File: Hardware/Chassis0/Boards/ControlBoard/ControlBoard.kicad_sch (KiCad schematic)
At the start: 18 parts, among them J1 TBP02R2W-381-06BE, J11 Conn_02x10_Counter_Clockwise, J12 Conn_02x10_Counter_Clockwise, J13 Conn_02x10_Counter_Clockwise, J14 Conn_02x10_Counter_Clockwise, J2 TBP02R2W-381-06BE, J3 TBP01R2W-508-02BE, J4 TBP01R1-508-04BE, J5 Conn_02x10_Counter_Clockwise, J7 TBP02R2W-381-08BE, J8 TBP02R2W-381-08BE

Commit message: Update size 0 cad model
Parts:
- removed J11, J12, J13, J14, J5: Conn_02x10_Counter_Clockwise, Connector_PinSocket_2.54mm:PinSocket_2x10_P2.54mm_Vertical, symbol Connector_Generic:Conn_02x10_Counter_Clockwise
- removed J4: TBP01R1-508-04BE, InverterCom:TBP01R150804BE, symbol InverterCom:TBP01R1-508-04BE
- removed J8: TBP02R2W-381-08BE, InverterCom:TBP02R2W38108BE, symbol InverterCom:TBP02R2W-381-08BE
- added J5, J6, J8, J9: Conn_02x08_Counter_Clockwise, Connector_PinSocket_2.54mm:PinSocket_2x08_P2.54mm_Vertical, symbol Connector_Generic:Conn_02x08_Counter_Clockwise
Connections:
- net HEATSINK_TMP_V: now also J9.16 (Pin_16)
- net CAN/CAN_L_B: now reaches J7.3
- net CAN/CAN_JMP_B: now reaches J7.5
- net +5V_V renamed +5V_C
- net +5V_C: now also J9.14 (Pin_14)
- net CAN_24V_OUT renamed CAN/CAN_JMP_A
- net CAN_GND: no longer names the net of J7.8
- net CAN_HIGH: no longer names the net of J7.7
- net CAN_JUMPER_A renamed CAN/CAN_H_B
- net CAN_JUMPER_B renamed CAN/CAN_GND
- net CAN_LOW: no longer names the net of J7.6
- net GND_V renamed GND_C
- net GND_C: now also J9.1 (Pin_1)
- new net +5V_Y: J9.4 (Pin_4)
- new net DC_LINK_VSENSE_U: J5.16 (Pin_16)
- new net GND_U: J5.4 (Pin_4)
- new net GND_Y: J9.2 (Pin_2)
- new net ISENSE_DC_LINK_Y: J9.6 (Pin_6)
- new net ISENSE_PH_U_Y: J9.8 (Pin_8)
- new net ISENSE_PH_V_Y: J9.10 (Pin_10)
- new net ISENSE_PH_W_Y: J9.12 (Pin_12)
- new net PH_U_H_G: J5.12 (Pin_12)
- new net PH_U_H_S: J5.14 (Pin_14)
- new net PH_U_L_D: J5.6 (Pin_6)
- new net PH_U_L_G: J5.2 (Pin_2)
- new net PH_V_H_D: J6.16 (Pin_16)
- new net PH_V_H_G: J6.12 (Pin_12)
- new net PH_V_H_S: J6.14 (Pin_14)
- new net PH_V_L_D: J6.6 (Pin_6)
- new net PH_V_L_G: J6.2 (Pin_2)
- new net PH_V_L_S: J6.4 (Pin_4)
- new net PH_W_H_D: J8.16 (Pin_16)
- new net PH_W_H_G: J8.12 (Pin_12)
- new net PH_W_H_S: J8.14 (Pin_14)
- new net PH_W_L_D: J8.6 (Pin_6)
- new net PH_W_L_G: J8.2 (Pin_2)
- new net PH_W_L_S: J8.4 (Pin_4)
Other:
- added sheet ADC_1 (ADC1.kicad_sch)
- added sheet CAN (CAN.kicad_sch)
- added sheet GateDriverAssembly (GateDriverAssembly.kicad_sch)
- sheet Control ports: added none; removed RELAY1_A, RELAY2_A, RELAY3_A
- note removed: "CANBUS OUTPUT CONNECTOR TO CONTROL BOARD INTERFACES TO OUTSIDE WORLD"
- note removed: "CONNECTION FROM MAINBOARD TO CONTROL MODULE ABOVE PROVIDES RELAY OUTPUTS + GATE DRIVER INTERLOCK"
- note removed: "CONNECTOR FROM MAIN BOARD TO CONTROL MODULE ABOVE ADC SPI INPUTS / POWER TO ADCS"
- note removed: "CONNECTOR FROM MAIN BOARD TO CONTROL MODULE ABOVE ADC SPI INPUTS / POWER TO ADCS / GATE DRIVE SIGNALS"
- note removed: "CONNECTOR FROM MAIN BOARD TO CONTROL MODULE ABOVE CONTROL INPUTS + POWER TO RELAY SUBSYSTEM/GATE DRIVERS"
- moved on the sheet: H1, H3, H4, H5, H7, H8, J2, J3, J7, R13

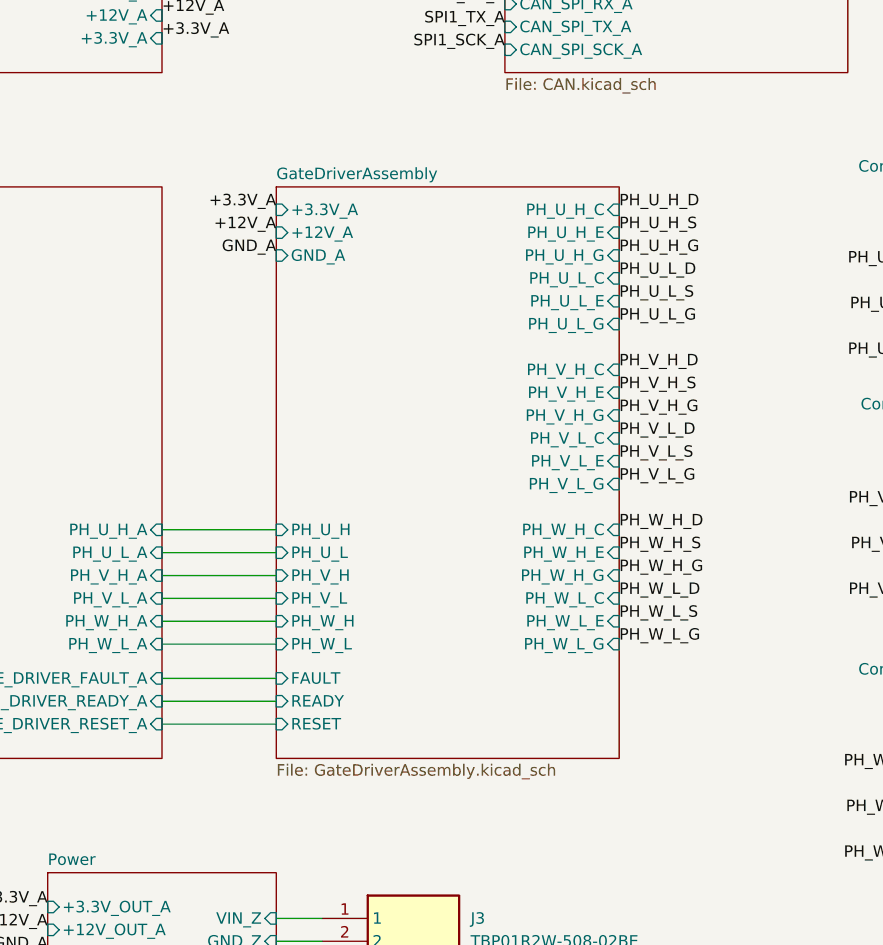
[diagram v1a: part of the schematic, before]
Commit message: Add control board outline for size 0
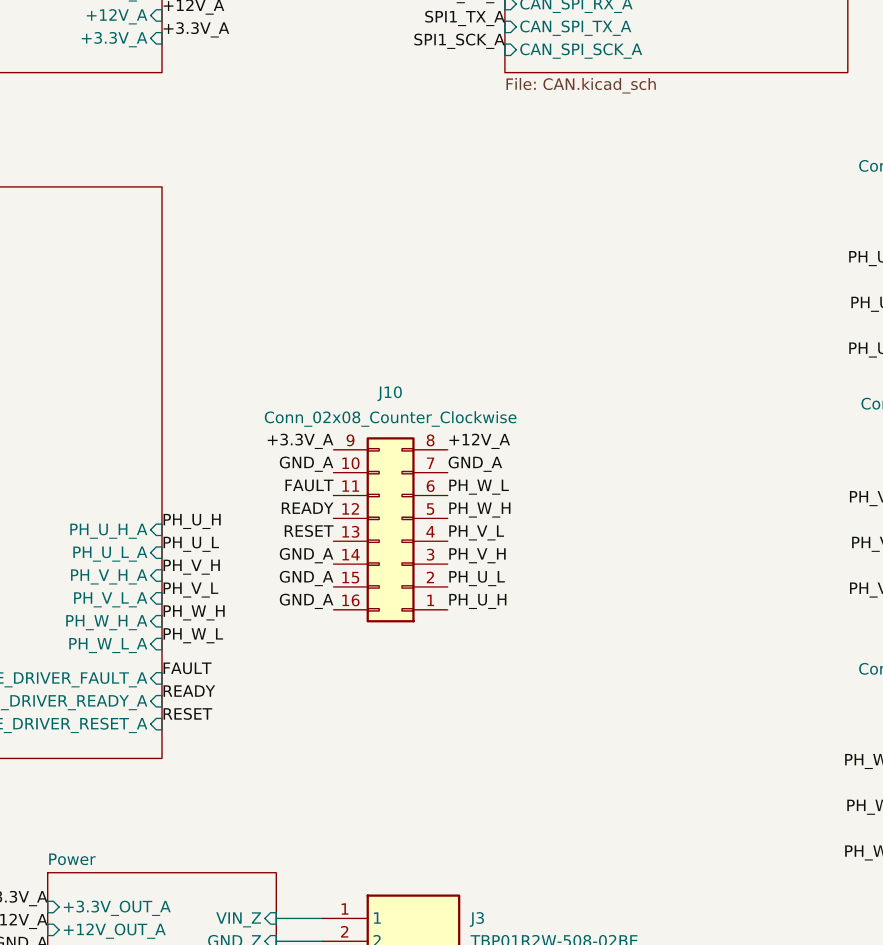
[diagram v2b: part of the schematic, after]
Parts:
- added J10: Conn_02x08_Counter_Clockwise, Connector_PinSocket_2.54mm:PinSocket_2x08_P2.54mm_Vertical, symbol Connector_Generic:Conn_02x08_Counter_Clockwise
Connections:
- net +12V_A: now also J10.8 (Pin_8)
- net +3.3V_A: now also J10.9 (Pin_9)
- net GND_A: now also J10.10 (Pin_10), J10.14 (Pin_14), J10.15 (Pin_15), J10.16 (Pin_16), J10.7 (Pin_7)
- new net FAULT: J10.11 (Pin_11)
- new net PH_U_H: J10.1 (Pin_1)
- new net PH_U_L: J10.2 (Pin_2)
- new net PH_V_H: J10.3 (Pin_3)
- new net PH_V_L: J10.4 (Pin_4)
- new net PH_W_H: J10.5 (Pin_5)
- new net PH_W_L: J10.6 (Pin_6)
- new net READY: J10.12 (Pin_12)
- new net RESET: J10.13 (Pin_13)
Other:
- removed sheet GateDriverAssembly

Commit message: finish chassis 0 board design v1
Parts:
- removed H5, H8: MountingHole, MountingHole:MountingHole_4.3mm_M4, symbol Mechanical:MountingHole
- removed H7: MountingHole, MountingHole:MountingHole_3.2mm_M3, symbol Mechanical:MountingHole
- added H2, H6, H9: MountingHole, MountingHole:MountingHole_4.3mm_M4, symbol Mechanical:MountingHole
- H1: footprint MountingHole:MountingHole_3.2mm_M3 -> MountingHole:MountingHole_4.3mm_M4
